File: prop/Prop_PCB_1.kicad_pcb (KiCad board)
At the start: 4 copper layers, 63.5 x 63.5 mm, 18 parts, among them J1 1984989, J2 1984989, J3 1984989, J4 1984989, J5 CAS_stacking, J6 Conn_01x02, J7 1984989, U1 L298P, U1301 MAX6675ISA+, U2 SN74LVC8T245DBR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

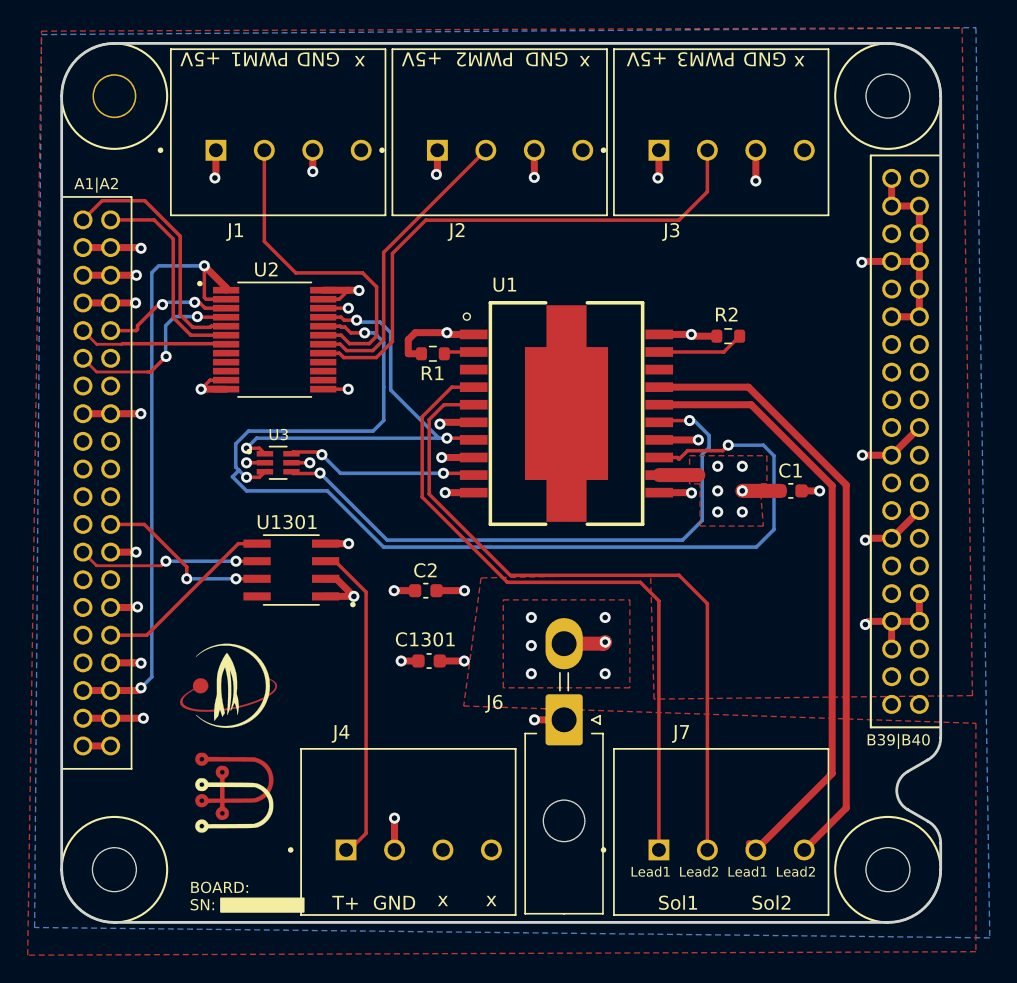
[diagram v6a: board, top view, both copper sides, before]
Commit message: Fixed power pours.
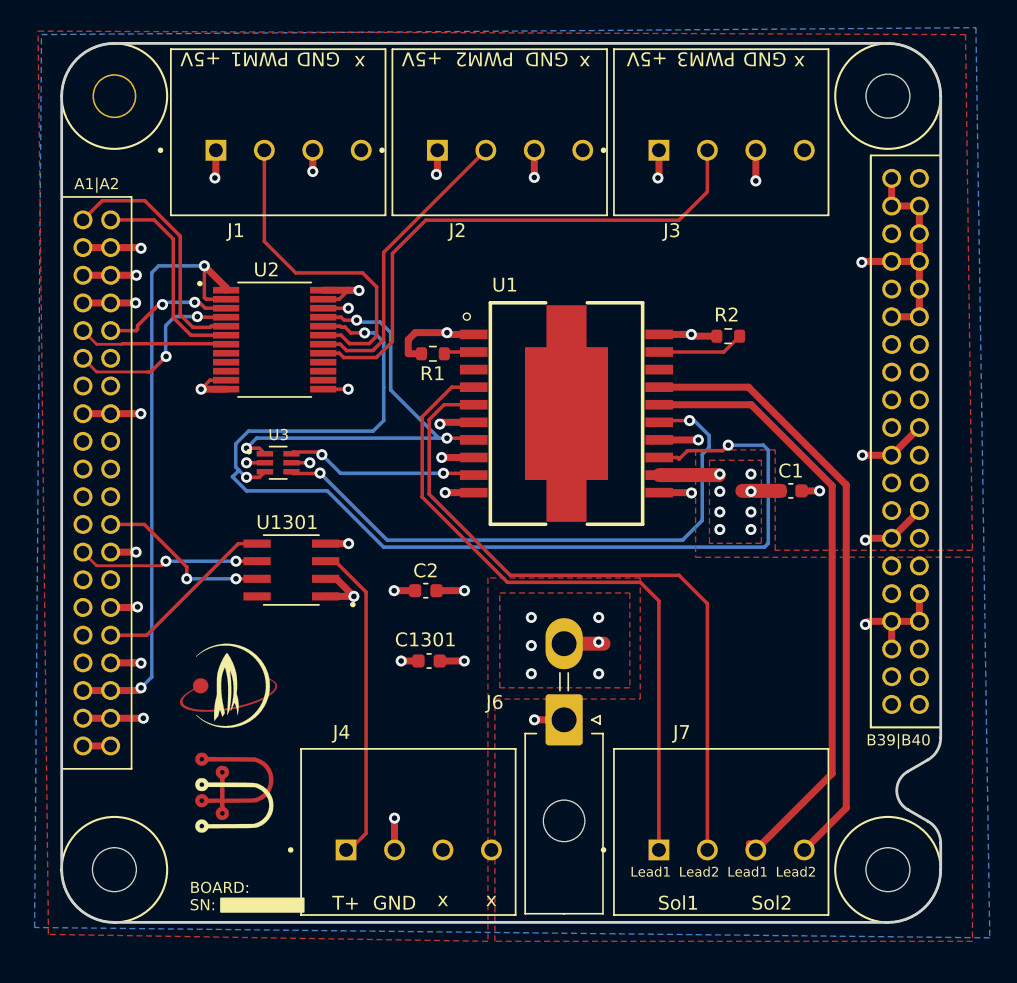
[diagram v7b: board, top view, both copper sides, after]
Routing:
- net +24V: track 8.39 -> 9.71 mm, vias 12 -> 14
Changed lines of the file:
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@@
   (segment (start 72.755238 74.347841) (end 74.099397 75.692) (width 0.254) (layer "B.Cu") (net 13))
   (segment (start 97.124 75.819) (end 99.949 75.819) (width 1.016) (layer "F.Cu") (net 14))
-  (segment (start 93.103 87.999) (end 93.218 87.884) (width 1.016) (layer "F.Cu") (net 14))
   (segment (start 105.853 76.96) (end 103.126 76.96) (width 1.016) (layer "F.Cu") (net 14))
+  (segment (start 99.949 75.819) (end 101.431 75.819) (width 1.016) (layer "F.Cu") (net 14))
   (segment (start 90.424 87.999) (end 93.103 87.999) (width 1.016) (layer "F.Cu") (net 14))
-  (via (at 93.218 90.17) (size 0.8) (drill 0.4) (layers "F.Cu" "B.Cu") (net 14))
+  (via (at 92.75 90.17) (size 0.8) (drill 0.4) (layers "F.Cu" "B.Cu") (net 14))
   (via (at 87.884 90.17) (size 0.8) (drill 0.4) (layers "F.Cu" "B.Cu") (net 14))
-  (via (at 101.346 78.486) (size 0.8) (drill 0.4) (layers "F.Cu" "B.Cu") (net 14))
-  (via (at 103.124 78.486) (size 0.8) (drill 0.4) (layers "F.Cu" "B.Cu") (net 14))
-  (via (at 103.124 75.184) (size 0.8) (drill 0.4) (layers "F.Cu" "B.Cu") (net 14))
-  (via (at 93.218 87.884) (size 0.8) (drill 0.4) (layers "F.Cu" "B.Cu") (net 14))
-  (via (at 101.346 75.184) (size 0.8) (drill 0.4) (layers "F.Cu" "B.Cu") (net 14))
-  (via (at 93.218 86.106) (size 0.8) (drill 0.4) (layers "F.Cu" "B.Cu") (net 14))
-  (via (at 103.126 76.96) (size 0.8) (drill 0.4) (layers "F.Cu" "B.Cu") (net 14))
+  (via (at 103.75 79.75) (size 0.8) (drill 0.4) (layers "F.Cu" "B.Cu") (net 14))
+  (via (at 101.5 78.486) (size 0.8) (drill 0.4) (layers "F.Cu" "B.Cu") (net 14))
+  (via (at 103.75 78.486) (size 0.8) (drill 0.4) (layers "F.Cu" "B.Cu") (net 14))
+  (via (at 103.75 75.75) (size 0.8) (drill 0.4) (layers "F.Cu" "B.Cu") (net 14))
+  (via (at 92.75 87.884) (size 0.8) (drill 0.4) (layers "F.Cu" "B.Cu") (net 14))
+  (via (at 101.5 75.75) (size 0.8) (drill 0.4) (layers "F.Cu" "B.Cu") (net 14))
+  (via (at 92.75 86.106) (size 0.8) (drill 0.4) (layers "F.Cu" "B.Cu") (net 14))
+  (via (at 103.75 77) (size 0.8) (drill 0.4) (layers "F.Cu" "B.Cu") (net 14))
   (via (at 87.884 88.138) (size 0.8) (drill 0.4) (layers "F.Cu" "B.Cu") (net 14))
-  (via (at 101.346 76.962) (size 0.8) (drill 0.4) (layers "F.Cu" "B.Cu") (net 14))
+  (via (at 101.5 77) (size 0.8) (drill 0.4) (layers "F.Cu" "B.Cu") (net 14))
   (via (at 87.884 86.106) (size 0.8) (drill 0.4) (layers "F.Cu" "B.Cu") (net 14))
+  (via (at 101.5 79.75) (size 0.8) (drill 0.4) (layers "F.Cu" "B.Cu") (net 14))
   (segment (start 101.712489 74.055511) (end 99.172489 74.055511) (width 0.254) (layer "F.Cu") (net 15))
   (segment (start 68.636 75.58) (end 68.236497 75.979503) (width 0.254) (layer "F.Cu") (net 15))
@@
   (via (at 102.108 73.66) (size 0.8) (drill 0.4) (layers "F.Cu" "B.Cu") (net 15))
   (via (at 75.841268 65.5465) (size 0.8) (drill 0.4) (layers "F.Cu" "B.Cu") (net 15))
-  (segment (start 105.41 79.756) (end 105.41 74.422) (width 0.254) (layer "B.Cu") (net 15))
   (segment (start 77.220481 66.22705) (end 76.539931 65.5465) (width 0.254) (layer "B.Cu") (net 15))
   (segment (start 66.760923 75.479077) (end 66.533489 75.251642) (width 0.254) (layer "B.Cu") (net 15))
   (segment (start 67.26135 75.979503) (end 66.760923 75.479077) (width 0.254) (layer "B.Cu") (net 15))
-  (segment (start 77.211519 81.021519) (end 104.144481 81.021519) (width 0.254) (layer "B.Cu") (net 15))
-  (segment (start 104.144481 81.021519) (end 105.41 79.756) (width 0.254) (layer "B.Cu") (net 15))
+  (segment (start 67.31 76.962) (end 73.152 76.962) (width 0.254) (layer "B.Cu") (net 15))
+  (segment (start 77.211519 81.021519) (end 104.728481 81.021519) (width 0.254) (layer "B.Cu") (net 15))
   (segment (start 66.533489 73.558855) (end 67.448344 72.644) (width 0.254) (layer "B.Cu") (net 15))
   (segment (start 77.22048 71.87752) (end 77.220481 69.469588) (width 0.254) (layer "B.Cu") (net 15))
   (segment (start 66.294 75.946) (end 67.31 76.962) (width 0.254) (layer "B.Cu") (net 15))
   (segment (start 75.7065 65.5465) (end 75.841268 65.5465) (width 0.254) (layer "B.Cu") (net 15))
-  (segment (start 67.31 76.962) (end 73.152 76.962) (width 0.254) (layer "B.Cu") (net 15))
-  (segment (start 105.41 74.422) (end 104.648 73.66) (width 0.254) (layer "B.Cu") (net 15))
   (segment (start 77.220481 69.469588) (end 77.220481 66.22705) (width 0.254) (layer "B.Cu") (net 15))
+  (segment (start 105 74.012) (end 104.648 73.66) (width 0.254) (layer "B.Cu") (net 15))
   (segment (start 66.533489 75.251642) (end 66.533489 73.558855) (width 0.254) (layer "B.Cu") (net 15))
   (segment (start 67.448344 72.644) (end 76.454 72.644) (width 0.254) (layer "B.Cu") (net 15))
+  (segment (start 66.760923 75.479077) (end 66.294 75.946) (width 0.254) (layer "B.Cu") (net 15))
+  (segment (start 104.648 73.66) (end 102.108 73.66) (width 0.254) (layer "B.Cu") (net 15))
+  (segment (start 105 80.75) (end 105 74.012) (width 0.254) (layer "B.Cu") (net 15))
+  (segment (start 73.152 76.962) (end 77.211519 81.021519) (width 0.254) (layer "B.Cu") (net 15))
+  (segment (start 104.728481 81.021519) (end 105 80.75) (width 0.254) (layer "B.Cu") (net 15))
   (segment (start 76.454 72.644) (end 77.22048 71.87752) (width 0.254) (layer "B.Cu") (net 15))
   (segment (start 67.31 75.979503) (end 67.26135 75.979503) (width 0.254) (layer "B.Cu") (net 15))
   (segment (start 76.539931 65.5465) (end 75.7065 65.5465) (width 0.254) (layer "B.Cu") (net 15))
-  (segment (start 73.152 76.962) (end 77.211519 81.021519) (width 0.254) (layer "B.Cu") (net 15))
-  (segment (start 104.648 73.66) (end 102.108 73.66) (width 0.254) (layer "B.Cu") (net 15))
-  (segment (start 66.760923 75.479077) (end 66.294 75.946) (width 0.254) (layer "B.Cu") (net 15))
   (segment (start 70.556 75.58) (end 70.682511 75.706511) (width 0.254) (layer "F.Cu") (net 16))
   (segment (start 99.314 71.882) (end 97.251 71.882) (width 0.254) (layer "F.Cu") (net 16))
@@
   (segment (start 70.866 61.214) (end 68.596 58.944) (width 0.254) (layer "F.Cu") (net 35))
   (segment (start 57.495 95.3849) (end 55.495 95.3849) (width 0.508) (layer "F.Cu") (net 42))
+  (zone (net 14) (net_name "+24V") (layer "F.Cu") (hatch edge 0.508)
+    (connect_pads (clearance 0.508))
+    (min_thickness 0.254) (filled_areas_thickness no)
+    (fill yes (thermal_gap 0.508) (thermal_bridge_width 0.508))
+    (polygon
+      (pts
+        (xy 95 91.186)
+        (xy 85.606 91.186)
+        (xy 85.606 84.336)
+        (xy 95 84.336)
+      )
+    )
+  )
   (zone (net 1) (net_name "GND") (layer "F.Cu") (hatch edge 0.508)
     (connect_pads (clearance 0.508))
@@
     (polygon
       (pts
-        (xy 119.75 91.75)
-        (xy 96.75 92)
-        (xy 96.5 83)
-        (xy 84.25 83.25)
-        (xy 83 92.5)
-        (xy 120 93.75)
-        (xy 120 110.25)
-        (xy 51.5 110.5)
-        (xy 52.5 43.75)
-        (xy 119 43.5)
+        (xy 119.25 44)
+        (xy 119.75 81.25)
+        (xy 105.5 81.25)
+        (xy 105.5 74)
+        (xy 99.75026 74.008064)
+        (xy 99.75052 81.758064)
+        (xy 119.75 81.75)
+        (xy 119.75 109.5)
+        (xy 85.25 109.5)
+        (xy 85.25 92)
+        (xy 95.75 92)
+        (xy 95.75 83.25)
+        (xy 84.75 83.25)
+        (xy 84.75 109.5)
+        (xy 53 109)
+        (xy 52.25 43.75)
       )
     )
@@
     (polygon
       (pts
-        (xy 95 91.186)
-        (xy 85.856 91.186)
-        (xy 85.856 84.836)
-        (xy 95 84.836)
-      )
-    )
-  )
-  (zone (net 14) (net_name "+24V") (layer "F.Cu") (hatch edge 0.508)
-    (connect_pads (clearance 0.508))
-    (min_thickness 0.254) (filled_areas_thickness no)
-    (fill yes (thermal_gap 0.508) (thermal_bridge_width 0.508))
-    (polygon
-      (pts
-        (xy 104.902 76.454)
-        (xy 104.394 76.454)
-        (xy 104.648 79.502)
-        (xy 100.076 79.502)
-        (xy 100.076 76.454)
-        (xy 99.314 76.454)
-        (xy 99.314 74.422)
-        (xy 104.902 74.422)
+        (xy 104.5 80.75)
+        (xy 100.75 80.75)
+        (xy 100.75 74.75)
+        (xy 104.5 74.75)
       )
     )
@@
     (polygon
       (pts
-        (xy 105 108.75)
+        (xy 104.75 108.75)
         (xy 85.5 108.75)
-        (xy 85.5 74.5)
-        (xy 105 74.5)
+        (xy 85.75 74.75)
+        (xy 105 74.75)
       )
     )
@@
     (polygon
       (pts
-        (xy 117.348 42.672)
-        (xy 117.856 107.696)
-        (xy 106.68 108.204)
-        (xy 105.918 73.406)
-        (xy 105.156 73.66)
-        (xy 104.648 73.914)
-        (xy 84.582 73.66)
-        (xy 84.328 85.344)
-        (xy 83.82 108.966)
-        (xy 52.07 109.22)
-        (xy 51.308 42.418)
-      )
-    )
+        (xy 118.25 108.75)
+        (xy 105.499948 108.753597)
+        (xy 105.999948 74.003597)
+        (xy 85.000052 73.996378)
+        (xy 84.500052 108.496378)
+        (xy 53.5 108.5)
+        (xy 53.5 44)
+        (xy 118.25 44)
+      )
+    )
